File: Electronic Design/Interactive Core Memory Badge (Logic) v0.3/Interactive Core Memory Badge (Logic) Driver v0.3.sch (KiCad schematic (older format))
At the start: 68 parts, among them J1 Conn_01x16_Female, J2 Conn_01x16_Female, Q10 MMBT4401LT1G, Q11 MMBT4403LT1G, Q12 MMBT4401LT1G, Q13 MMBT4403LT1G, Q14 MMBT4401LT1G, Q15 MMBT4403LT1G, Q16 MMBT4401LT1G, Q17 MMBT4403LT1G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

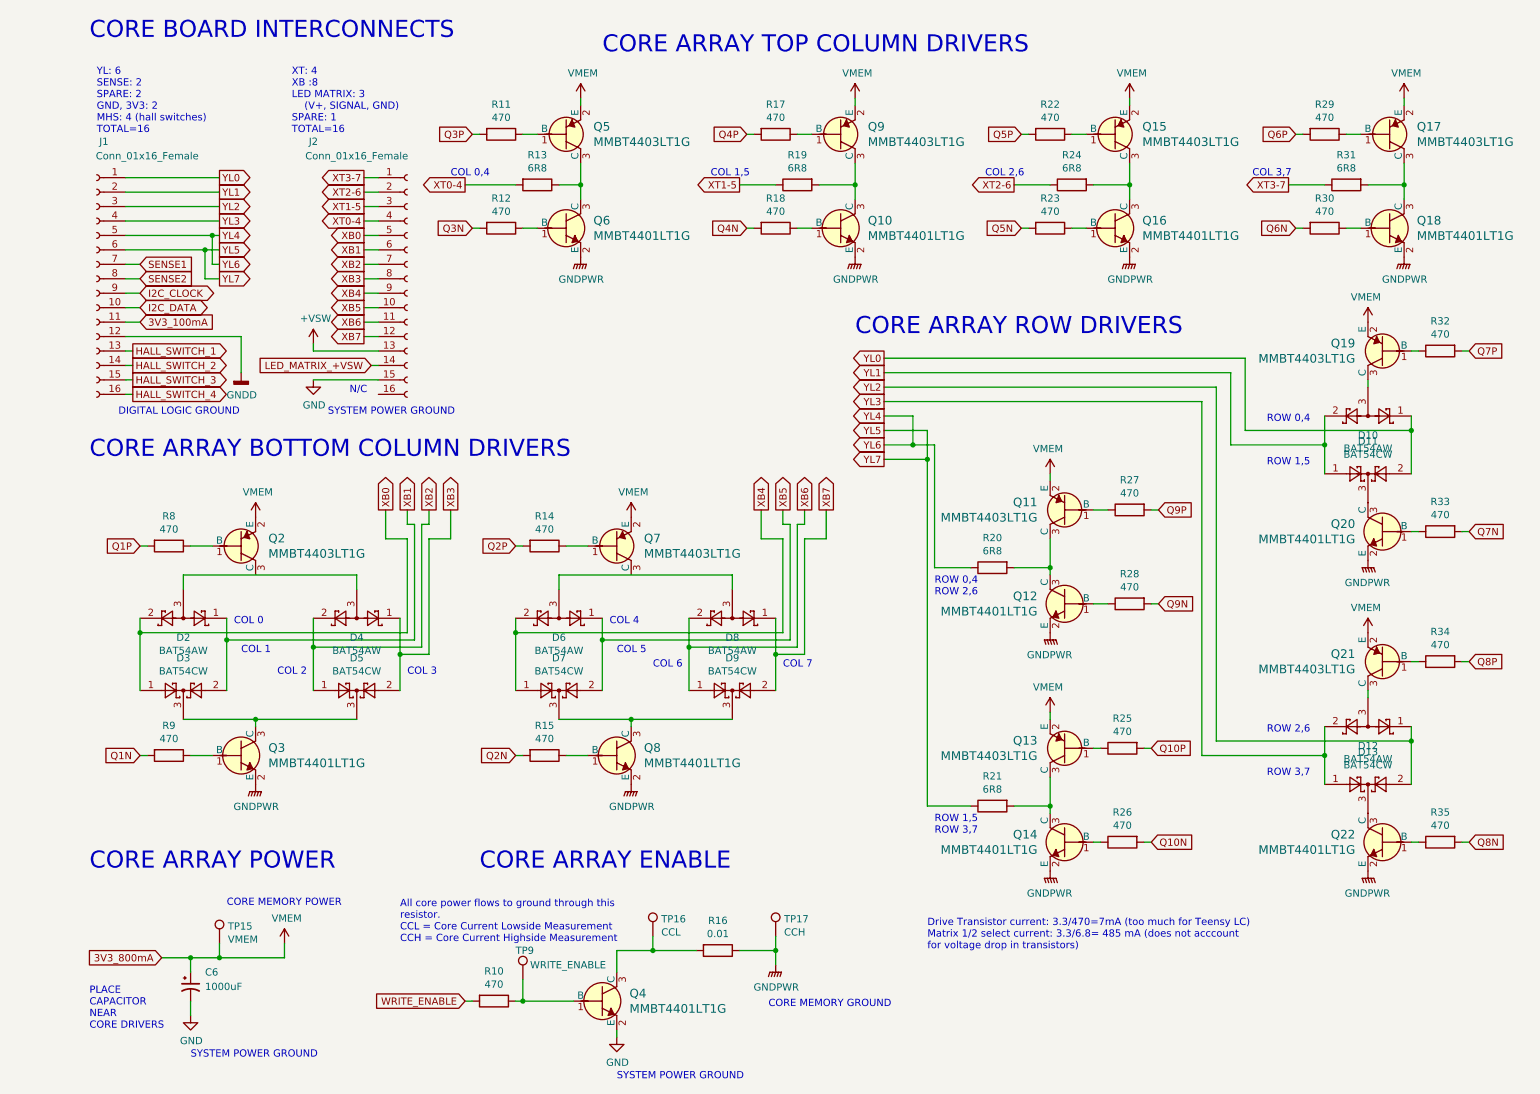
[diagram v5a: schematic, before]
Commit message: Schematic refinement, header position checks.
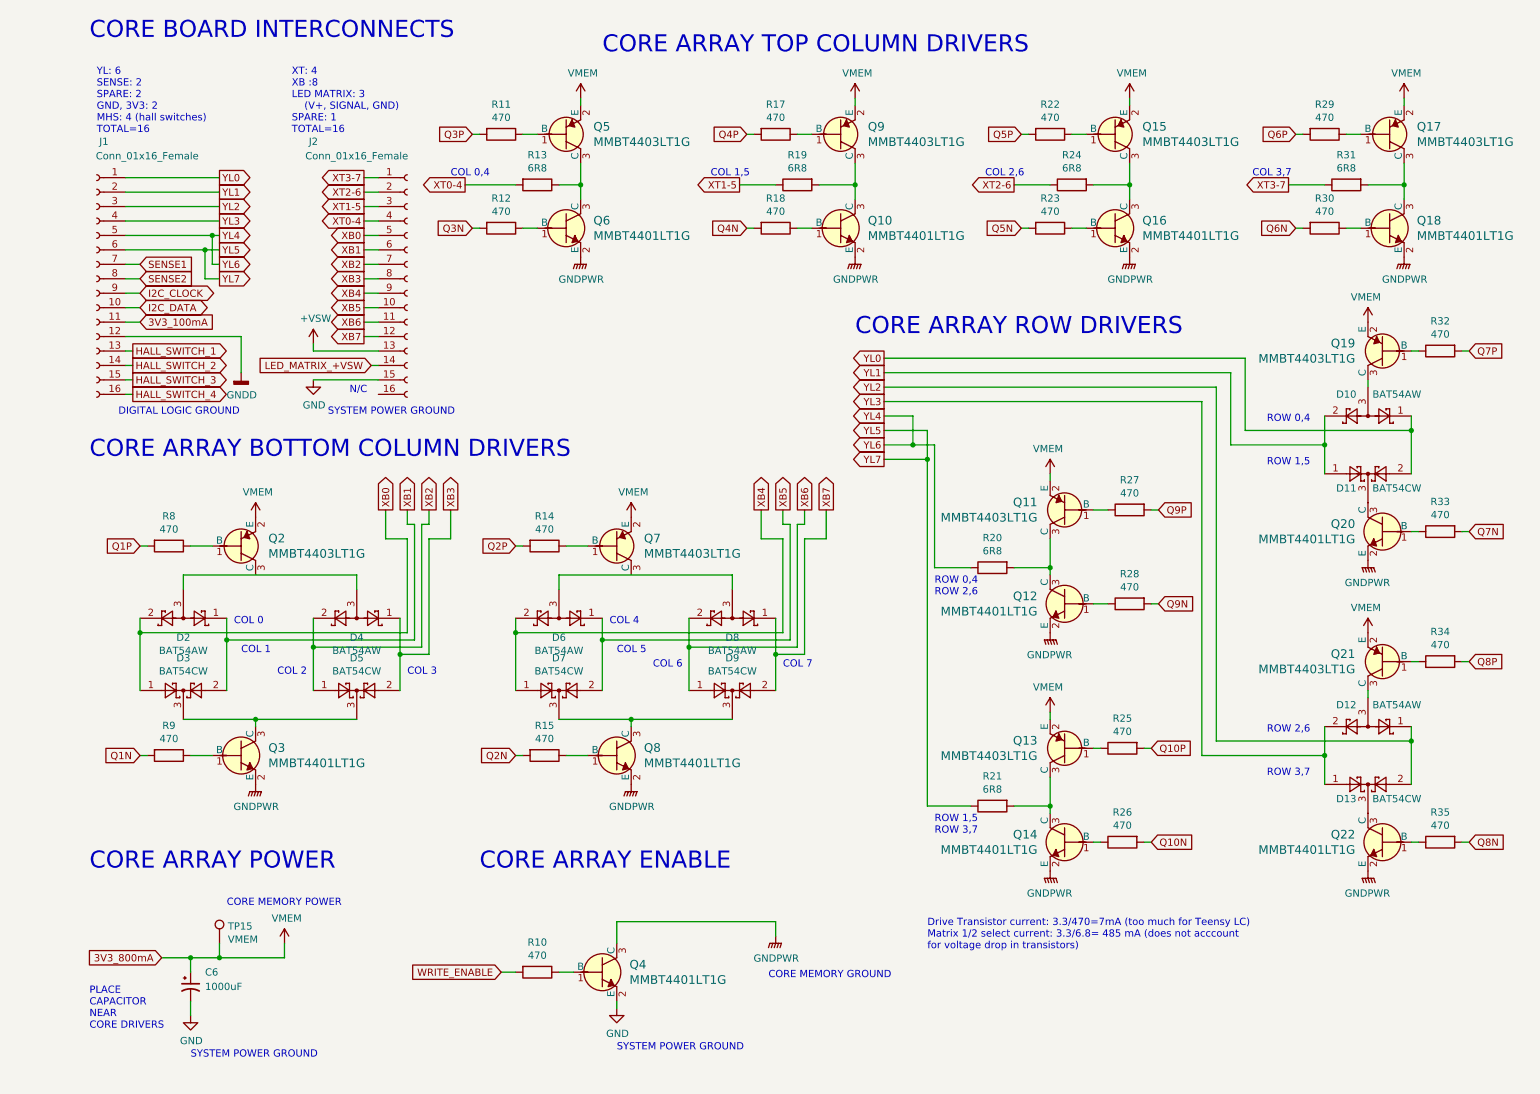
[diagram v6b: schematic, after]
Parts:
- removed R16: 0.01, Resistor_SMD:R_0805_2012Metric, symbol Device:R
- removed TP16: CCL, TestPoint:TestPoint_Keystone_5000-5004_Miniature, symbol Connector:TestPoint
- removed TP17: CCH, TestPoint:TestPoint_Keystone_5000-5004_Miniature, symbol Connector:TestPoint
- removed TP9: WRITE_ENABLE, TestPoint:TestPoint_Keystone_5000-5004_Miniature, symbol Connector:TestPoint
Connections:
- net GNDPWR: now also Q4.3 (C)
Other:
- note removed: "All core power flows to ground through this\nresistor.\nCCL = Core Current Lowside Measurement\nCCH = Core Current Highside Measurement"
- moved on the sheet: Q4, R10
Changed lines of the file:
@@
 U 1 1 5D5609D1
 P 9400 5500
-F 0 "D12" H 9400 5633 50  0000 C CNN
-F 1 "BAT54AW" H 9400 5724 50  0000 C CNN
+F 0 "D12" H 9550 5350 50  0000 C CNN
+F 1 "BAT54AW" H 9200 5350 50  0000 C CNN
 F 2 "Package_TO_SOT_SMD:SOT-323_SC-70" H 9475 5625 50  0001 L CNN
 F 3 "https://assets.nexperia.com/documents/data-sheet/BAT54W_SER.pdf" H 9280 5500 50  0001 C CNN
@@
 U 1 1 5D56153A
 P 9400 5900
-F 0 "D13" H 9400 6125 50  0000 C CNN
-F 1 "BAT54CW" H 9400 6034 50  0000 C CNN
+F 0 "D13" H 9250 5800 50  0000 C CNN
+F 1 "BAT54CW" H 9600 5800 50  0000 C CNN
 F 2 "Package_TO_SOT_SMD:SOT-323_SC-70" H 9475 6025 50  0001 L CNN
 F 3 "https://assets.nexperia.com/documents/data-sheet/BAT54W_SER.pdf" H 9320 5900 50  0001 C CNN
@@
 U 1 1 5D57DB50
 P 9400 3350
-F 0 "D10" H 9400 3483 50  0000 C CNN
-F 1 "BAT54AW" H 9400 3574 50  0000 C CNN
+F 0 "D10" H 9550 3200 50  0000 C CNN
+F 1 "BAT54AW" H 9200 3200 50  0000 C CNN
 F 2 "Package_TO_SOT_SMD:SOT-323_SC-70" H 9475 3475 50  0001 L CNN
 F 3 "https://assets.nexperia.com/documents/data-sheet/BAT54W_SER.pdf" H 9280 3350 50  0001 C CNN
@@
 U 1 1 5D57EB12
 P 9400 3750
-F 0 "D11" H 9400 3975 50  0000 C CNN
-F 1 "BAT54CW" H 9400 3884 50  0000 C CNN
+F 0 "D11" H 9250 3650 50  0000 C CNN
+F 1 "BAT54CW" H 9600 3650 50  0000 C CNN
 F 2 "Package_TO_SOT_SMD:SOT-323_SC-70" H 9475 3875 50  0001 L CNN
 F 3 "https://assets.nexperia.com/documents/data-sheet/BAT54W_SER.pdf" H 9320 3750 50  0001 C CNN
@@
 Text Notes 8700 5550 0    50   ~ 0
 ROW 2,6
-Text GLabel 3150 7400 0    50   Input ~ 0
+Text GLabel 3400 7200 0    50   Input ~ 0
 WRITE_ENABLE
-Text Notes 5250 7450 0    50   ~ 0
+Text Notes 5250 7250 0    50   ~ 0
 CORE MEMORY GROUND
 $Comp
 L Digikey-Transistors:MMBT4401LT1G Q?
 U 1 1 5E8ED55F
-P 4100 7400
+P 4100 7200
 AR Path="/5E8ED55F" Ref="Q?"  Part="1"
 AR Path="/5D254AE8/5E8ED55F" Ref="Q?"  Part="1"
 AR Path="/5E755AC8/5E8ED55F" Ref="Q4"  Part="1"
-F 0 "Q4" H 4288 7453 60  0000 L CNN
-F 1 "MMBT4401LT1G" H 4288 7347 60  0000 L CNN
-F 2 "Digikey:SOT-23-3" H 4300 7600 60  0001 L CNN
-F 3 "http://www.onsemi.com/pub/Collateral/MMBT4401LT1-D.PDF" H 4300 7700 60  0001 L CNN
-F 4 "MMBT4401LT1GOSCT-ND" H 4300 7800 60  0001 L CNN "Digi-Key_PN"
-F 5 "MMBT4401LT1G" H 4300 7900 60  0001 L CNN "MPN"
-F 6 "Discrete Semiconductor Products" H 4300 8000 60  0001 L CNN "Category"
-F 7 "Transistors - Bipolar (BJT) - Single" H 4300 8100 60  0001 L CNN "Family"
-F 8 "http://www.onsemi.com/pub/Collateral/MMBT4401LT1-D.PDF" H 4300 8200 60  0001 L CNN "DK_Datasheet_Link"
-F 9 "/product-detail/en/on-semiconductor/MMBT4401LT1G/MMBT4401LT1GOSCT-ND/1139819" H 4300 8300 60  0001 L CNN "DK_Detail_Page"
-F 10 "TRANS NPN 40V 0.6A SOT23" H 4300 8400 60  0001 L CNN "Description"
-F 11 "ON Semiconductor" H 4300 8500 60  0001 L CNN "Manufacturer"
-F 12 "Active" H 4300 8600 60  0001 L CNN "Status"
-	1    4100 7400
-	1    0    0    -1
-$EndComp
-Wire Wire Line
-	4200 7050 4200 7200
+F 0 "Q4" H 4288 7253 60  0000 L CNN
+F 1 "MMBT4401LT1G" H 4288 7147 60  0000 L CNN
+F 2 "Digikey:SOT-23-3" H 4300 7400 60  0001 L CNN
+F 3 "http://www.onsemi.com/pub/Collateral/MMBT4401LT1-D.PDF" H 4300 7500 60  0001 L CNN
+F 4 "MMBT4401LT1GOSCT-ND" H 4300 7600 60  0001 L CNN "Digi-Key_PN"
+F 5 "MMBT4401LT1G" H 4300 7700 60  0001 L CNN "MPN"
+F 6 "Discrete Semiconductor Products" H 4300 7800 60  0001 L CNN "Category"
+F 7 "Transistors - Bipolar (BJT) - Single" H 4300 7900 60  0001 L CNN "Family"
+F 8 "http://www.onsemi.com/pub/Collateral/MMBT4401LT1-D.PDF" H 4300 8000 60  0001 L CNN "DK_Datasheet_Link"
+F 9 "/product-detail/en/on-semiconductor/MMBT4401LT1G/MMBT4401LT1GOSCT-ND/1139819" H 4300 8100 60  0001 L CNN "DK_Detail_Page"
+F 10 "TRANS NPN 40V 0.6A SOT23" H 4300 8200 60  0001 L CNN "Description"
+F 11 "ON Semiconductor" H 4300 8300 60  0001 L CNN "Manufacturer"
+F 12 "Active" H 4300 8400 60  0001 L CNN "Status"
+	1    4100 7200
+	1    0    0    -1
+$EndComp
+Wire Wire Line
+	4200 6850 4200 7000
 $Comp
 L Device:R R?
 U 1 1 5E8ED566
-P 3350 7400
+P 3650 7200
 AR Path="/5E8ED566" Ref="R?"  Part="1"
 AR Path="/5D254AE8/5E8ED566" Ref="R?"  Part="1"
 AR Path="/5E755AC8/5E8ED566" Ref="R10"  Part="1"
-F 0 "R10" V 3143 7400 50  0000 C CNN
-F 1 "470" V 3234 7400 50  0000 C CNN
-F 2 "Resistor_SMD:R_0805_2012Metric" V 3280 7400 50  0001 C CNN
-F 3 "~" H 3350 7400 50  0001 C CNN
-	1    3350 7400
+F 0 "R10" V 3443 7200 50  0000 C CNN
+F 1 "470" V 3534 7200 50  0000 C CNN
+F 2 "Resistor_SMD:R_0805_2012Metric" V 3580 7200 50  0001 C CNN
+F 3 "~" H 3650 7200 50  0001 C CNN
+	1    3650 7200
 	0    1    1    0
 $EndComp
-Wire Wire Line
-	3500 7400 3550 7400
 $Comp
 L power:GNDPWR #PWR?
 U 1 1 5E8ED56D
-P 5300 7150
+P 5300 6950
 AR Path="/5E8ED56D" Ref="#PWR?"  Part="1"
 AR Path="/5D254AE8/5E8ED56D" Ref="#PWR?"  Part="1"
 AR Path="/5E755AC8/5E8ED56D" Ref="#PWR0151"  Part="1"
-F 0 "#PWR0151" H 5300 6950 50  0001 C CNN
-F 1 "GNDPWR" H 5304 6996 50  0000 C CNN
-F 2 "" H 5300 7100 50  0001 C CNN
-F 3 "" H 5300 7100 50  0001 C CNN
-	1    5300 7150
-	1    0    0    -1
-$EndComp
-Wire Wire Line
-	3150 7400 3200 7400
+F 0 "#PWR0151" H 5300 6750 50  0001 C CNN
+F 1 "GNDPWR" H 5304 6796 50  0000 C CNN
+F 2 "" H 5300 6900 50  0001 C CNN
+F 3 "" H 5300 6900 50  0001 C CNN
+	1    5300 6950
+	1    0    0    -1
+$EndComp
+Wire Wire Line
+	3400 7200 3500 7200
 Text Notes 1500 6750 0    50   ~ 0
 CORE MEMORY POWER
-$Comp
-L Device:R R?
-U 1 1 5E8ED580
-P 4900 7050
-AR Path="/5E8ED580" Ref="R?"  Part="1"
-AR Path="/5D254AE8/5E8ED580" Ref="R?"  Part="1"
-AR Path="/5E755AC8/5E8ED580" Ref="R16"  Part="1"
-F 0 "R16" V 4693 7050 50  0000 C CNN
-F 1 "0.01" V 4784 7050 50  0000 C CNN
-F 2 "Resistor_SMD:R_0805_2012Metric" V 4830 7050 50  0001 C CNN
-F 3 "~" H 4900 7050 50  0001 C CNN
-	1    4900 7050
-	0    1    1    0
-$EndComp
-Wire Wire Line
-	5050 7050 5300 7050
-$Comp
-L Connector:TestPoint TP?
-U 1 1 5E8ED587
-P 4450 6950
-AR Path="/5D254AE8/5E8ED587" Ref="TP?"  Part="1"
-AR Path="/5E8ED587" Ref="TP?"  Part="1"
-AR Path="/5E755AC8/5E8ED587" Ref="TP16"  Part="1"
-F 0 "TP16" H 4508 7068 50  0000 L CNN
-F 1 "CCL" H 4508 6977 50  0000 L CNN
-F 2 "TestPoint:TestPoint_Keystone_5000-5004_Miniature" H 4650 6950 50  0001 C CNN
-F 3 "~" H 4650 6950 50  0001 C CNN
-	1    4450 6950
-	1    0    0    -1
-$EndComp
-$Comp
-L Connector:TestPoint TP?
-U 1 1 5E8ED58D
-P 5300 6950
-AR Path="/5D254AE8/5E8ED58D" Ref="TP?"  Part="1"
-AR Path="/5E8ED58D" Ref="TP?"  Part="1"
-AR Path="/5E755AC8/5E8ED58D" Ref="TP17"  Part="1"
-F 0 "TP17" H 5358 7068 50  0000 L CNN
-F 1 "CCH" H 5358 6977 50  0000 L CNN
-F 2 "TestPoint:TestPoint_Keystone_5000-5004_Miniature" H 5500 6950 50  0001 C CNN
-F 3 "~" H 5500 6950 50  0001 C CNN
-	1    5300 6950
-	1    0    0    -1
-$EndComp
-Wire Wire Line
-	5300 6950 5300 7050
-Connection ~ 5300 7050
-Wire Wire Line
-	4450 6950 4450 7050
-Connection ~ 4450 7050
-Wire Wire Line
-	4450 7050 4750 7050
 Text GLabel 1050 7100 0    50   Input ~ 0
 3V3_800mA
@@
 L power:GND #PWR?
 U 1 1 5E8ED59A
-P 4200 7650
+P 4200 7450
 AR Path="/5D254AE8/5E8ED59A" Ref="#PWR?"  Part="1"
 AR Path="/5E8ED59A" Ref="#PWR?"  Part="1"
 AR Path="/5E755AC8/5E8ED59A" Ref="#PWR0152"  Part="1"
-F 0 "#PWR0152" H 4200 7400 50  0001 C CNN
-F 1 "GND" H 4205 7475 50  0000 C CNN
-F 2 "" H 4200 7650 50  0001 C CNN
-F 3 "" H 4200 7650 50  0001 C CNN
-	1    4200 7650
-	1    0    0    -1
-$EndComp
-Wire Wire Line
-	4200 7600 4200 7650
-Text Notes 2700 7000 0    50   ~ 0
-All core power flows to ground through this\nresistor.\nCCL = Core Current Lowside Measurement\nCCH = Core Current Highside Measurement
+F 0 "#PWR0152" H 4200 7200 50  0001 C CNN
+F 1 "GND" H 4205 7275 50  0000 C CNN
+F 2 "" H 4200 7450 50  0001 C CNN
+F 3 "" H 4200 7450 50  0001 C CNN
+	1    4200 7450
+	1    0    0    -1
+$EndComp
+Wire Wire Line
+	4200 7400 4200 7450
 Wire Wire Line
 	2600 4000 2600 4200
@@
 	5350 4200 5200 4200
 Wire Wire Line
-	5300 7050 5300 7150
+	5300 6850 5300 6950
 Connection ~ 6350 3650
 Wire Wire Line
@@
 Wire Wire Line
 	1900 7100 1900 7000
-Wire Wire Line
-	4200 7050 4450 7050
 Text Notes 3250 6500 0    118  ~ 0
 CORE ARRAY ENABLE
@@
 Text Notes 750  3350 0    50   ~ 0
 DIGITAL LOGIC GROUND
-Text Notes 4200 7950 0    50   ~ 0
+Text Notes 4200 7750 0    50   ~ 0
 SYSTEM POWER GROUND
 $Comp
@@
 Wire Wire Line
 	800  2600 900  2600
-$Comp
-L Connector:TestPoint TP?
-U 1 1 5E9A49E8
-P 3550 7250
-AR Path="/5E755787/5E9A49E8" Ref="TP?"  Part="1"
-AR Path="/5E755AC8/5D2551FF/5E9A49E8" Ref="TP?"  Part="1"
-AR Path="/5E755AC8/5E9A49E8" Ref="TP9"  Part="1"
-F 0 "TP9" H 3500 7450 50  0000 L CNN
-F 1 "WRITE_ENABLE" H 3600 7350 50  0000 L CNN
-F 2 "TestPoint:TestPoint_Keystone_5000-5004_Miniature" H 3750 7250 50  0001 C CNN
-F 3 "~" H 3750 7250 50  0001 C CNN
-	1    3550 7250
-	1    0    0    -1
-$EndComp
-Wire Wire Line
-	3550 7250 3550 7400
-Connection ~ 3550 7400
-Wire Wire Line
-	3550 7400 3900 7400
+Wire Wire Line
+	4200 6850 5300 6850
+Wire Wire Line
+	3800 7200 3900 7200
 $EndSCHEMATC

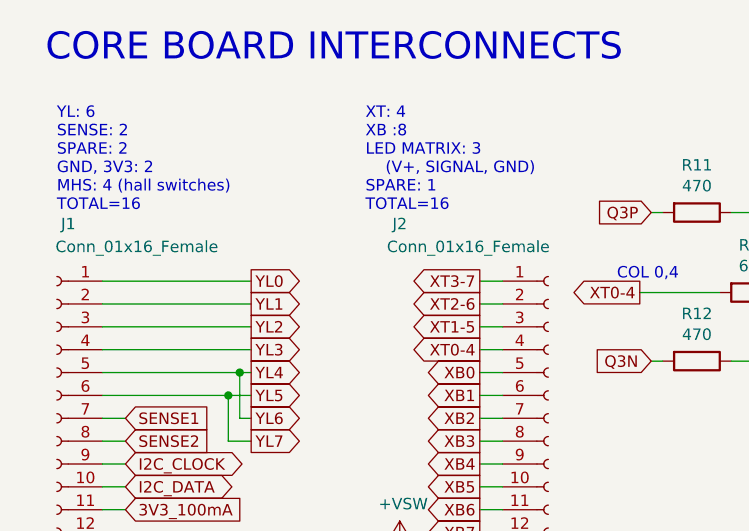
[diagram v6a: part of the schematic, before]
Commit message: Footprint verification and refinement
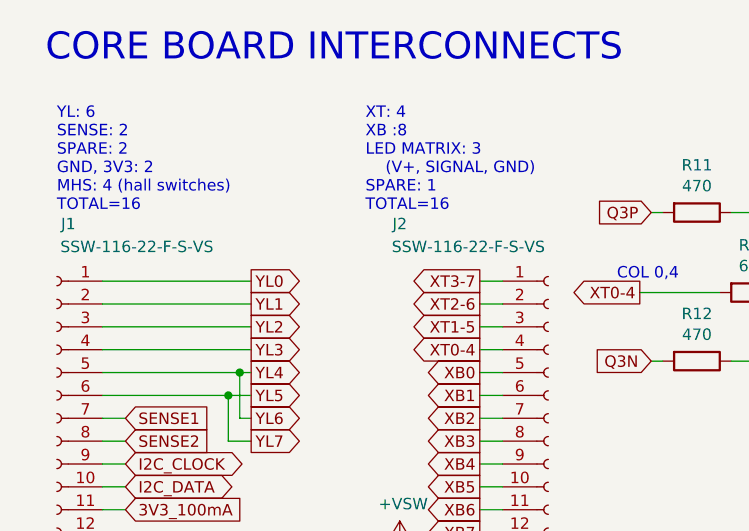
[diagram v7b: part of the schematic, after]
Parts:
- J1, J2: value Conn_01x16_Female -> SSW-116-22-F-S-VS‎
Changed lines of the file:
@@
 P 2750 2400
 F 0 "J2" H 2100 3350 50  0000 C CNN
-F 1 "Conn_01x16_Female" H 2400 3250 50  0000 C CNN
+F 1 "SSW-116-22-F-S-VS‎" H 2400 3250 50  0000 C CNN
 F 2 "Connector_PinHeader_2.54mm:PinHeader_1x16_P2.54mm_Vertical_SMD_and_TH_Pin1Left" H 2750 2400 50  0001 C CNN
 F 3 "~" H 2750 2400 50  0001 C CNN
@@
 P 600 2400
 F 0 "J1" H 550 3350 50  0000 C CNN
-F 1 "Conn_01x16_Female" H 250 3250 50  0000 C CNN
+F 1 "SSW-116-22-F-S-VS‎" H 250 3250 50  0000 C CNN
 F 2 "Connector_PinHeader_2.54mm:PinHeader_1x16_P2.54mm_Vertical_SMD_and_TH_Pin1Left" H 600 2400 50  0001 C CNN
 F 3 "~" H 600 2400 50  0001 C CNN

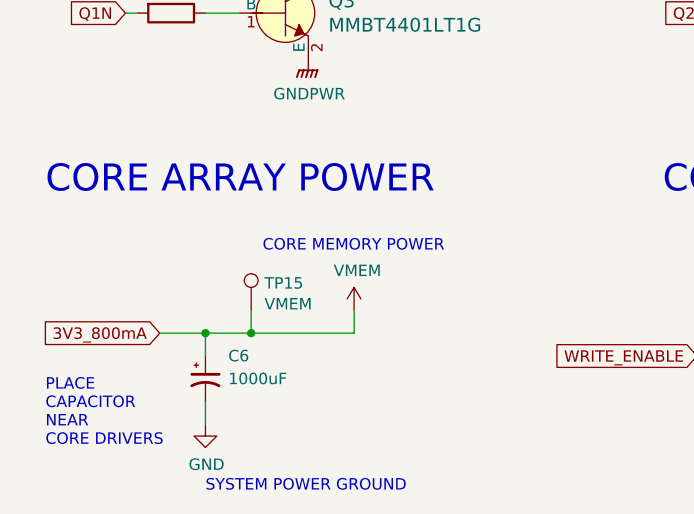
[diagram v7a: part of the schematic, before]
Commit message: Embiggen to 85x170mm
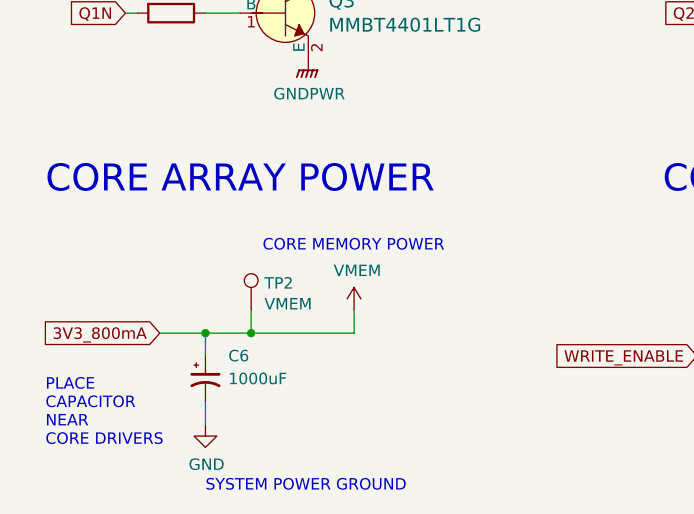
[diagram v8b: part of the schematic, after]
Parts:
- TP2: renamed from TP15; footprint TestPoint:TestPoint_Keystone_5000-5004_Miniature -> TestPoint:TestPoint_THTPad_D1.7mm_Drill1.0mm
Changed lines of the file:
@@
 AR Path="/5D254AE8/5E8ED577" Ref="TP?"  Part="1"
 AR Path="/5E8ED577" Ref="TP?"  Part="1"
-AR Path="/5E755AC8/5E8ED577" Ref="TP15"  Part="1"
-F 0 "TP15" H 1508 7118 50  0000 L CNN
+AR Path="/5E755AC8/5E8ED577" Ref="TP2"  Part="1"
+F 0 "TP2" H 1508 7118 50  0000 L CNN
 F 1 "VMEM" H 1508 7027 50  0000 L CNN
-F 2 "TestPoint:TestPoint_Keystone_5000-5004_Miniature" H 1650 7000 50  0001 C CNN
+F 2 "TestPoint:TestPoint_THTPad_D1.7mm_Drill1.0mm" H 1650 7000 50  0001 C CNN
 F 3 "~" H 1650 7000 50  0001 C CNN
 	1    1450 7000
